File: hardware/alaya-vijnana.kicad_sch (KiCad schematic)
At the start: 31 parts, among them J1 Debug/Flash, J3 Bat, J4 USB_C_Receptacle_USB2.0_16P, SW1 Reset, SW23 Power_Switch, U1 nRF52840_E73-2G4M08S1C, U6 BQ24075RGT, X2 32.768kHz

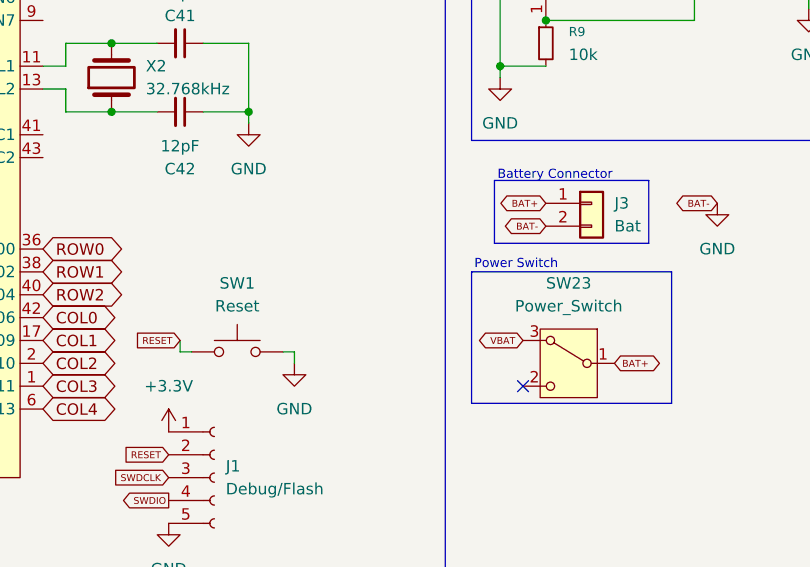
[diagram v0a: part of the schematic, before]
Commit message: started routing left side
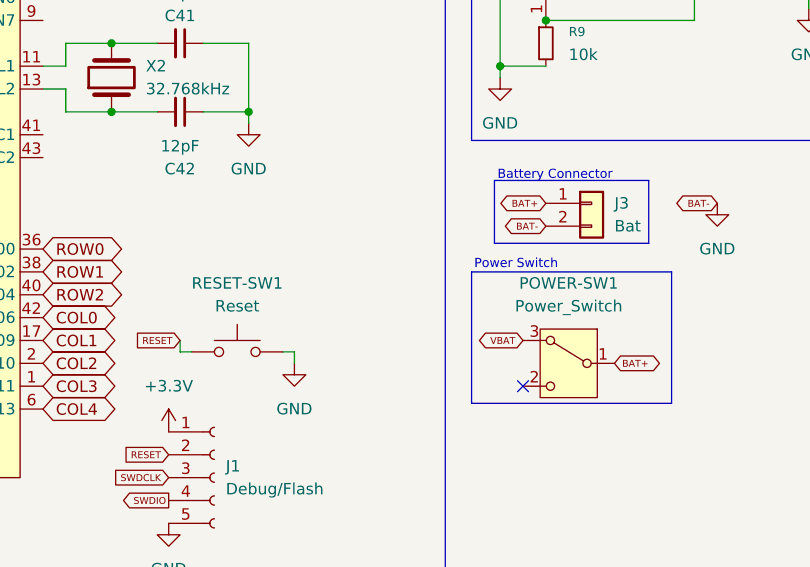
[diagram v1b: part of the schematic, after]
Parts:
- C2: footprint (none) -> Capacitor_SMD:C_0603_1608Metric_Pad1.08x0.95mm_HandSolder
- F1: footprint (none) -> Fuse:Fuse_0603_1608Metric_Pad1.05x0.95mm_HandSolder
- J1: footprint (none) -> Connector_PinSocket_2.00mm:PinSocket_1x05_P2.00mm_Vertical
- LED2: footprint PCM_LED_SMD_AKL:LED_1206_3216Metric -> LED_SMD:LED_0805_2012Metric_Pad1.15x1.40mm_HandSolder
- RESET-SW1: renamed from SW1; footprint (none) -> Button_Switch_SMD:SW_Push_1P1T_NO_CK_KMR2
- renumbered SW23 to POWER-SW1
